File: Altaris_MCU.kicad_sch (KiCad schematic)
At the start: 94 parts, among them J1 Screw_Terminal_01x02, J10 USB_C_Receptacle_USB2.0_16P, J11 Screw_Terminal_01x02, J12 Screw_Terminal_01x02, J13 Screw_Terminal_01x02, J14 Screw_Terminal_01x02, J15 Screw_Terminal_01x02, J16 Conn_01x06, J2 Screw_Terminal_01x02, J3 Screw_Terminal_01x02, J4 Screw_Terminal_01x02, J5 Screw_Terminal_01x02, J6 Screw_Terminal_01x02, J7 Conn_01x08_Socket, J8 Screw_Terminal_01x02, J9 USB_C_Receptacle_USB2.0_16P, Q1 Q_NMOS, SW2 RESET1, SW3 BOOT1, U1 ESP32-S3-WROOM-1, U10 USBLC6-2SC6, U11 MAX31855TASA, U12 TPS62827DMQT, U13 USBLC6-2SC6, U15 CH340X, U17 MAX31855TASA, U18 MAX31855TASA, U2 MAX31855KASA, U3 TPS79333-EP, U4 ICM-20948, U5 TPS79318-EP, U6 SN74AVC4T774RSVR, U7 MAX31855KASA, U8 MAX31855KASA, U9 SN74AVC4T774RSVR

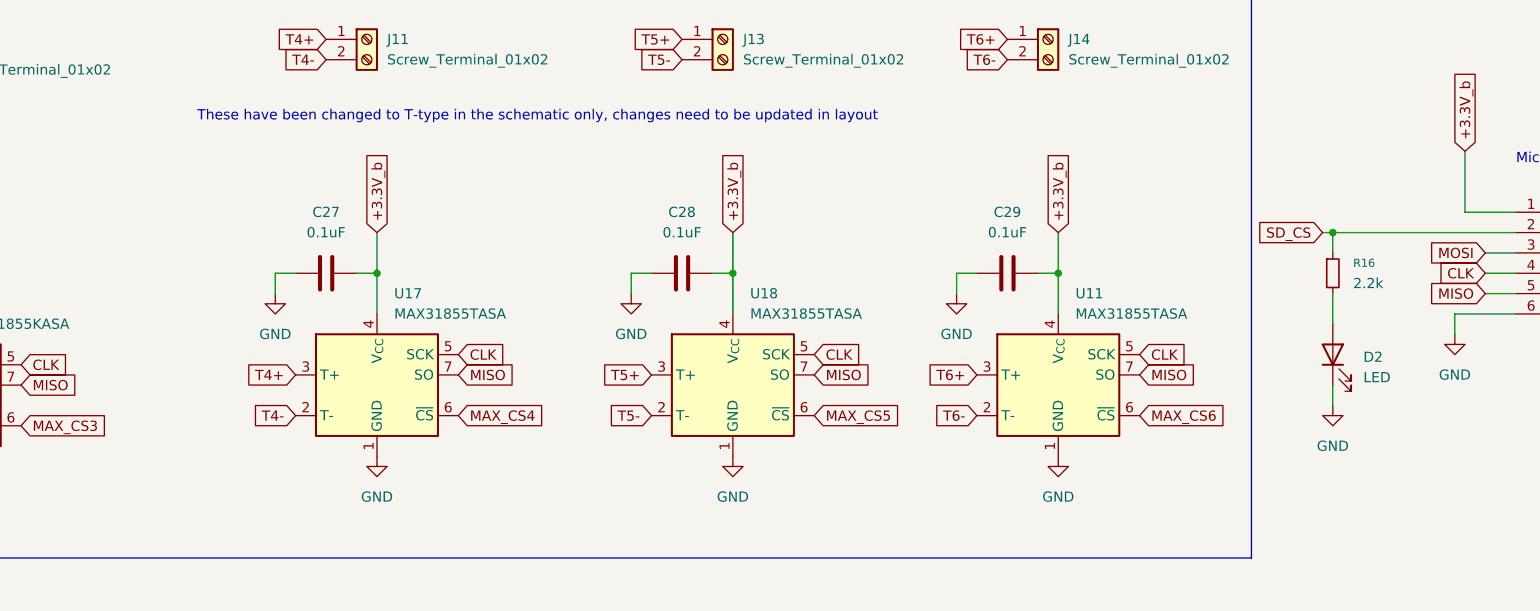
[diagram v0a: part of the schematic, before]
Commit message: added led to thermocouple power lines in schematic
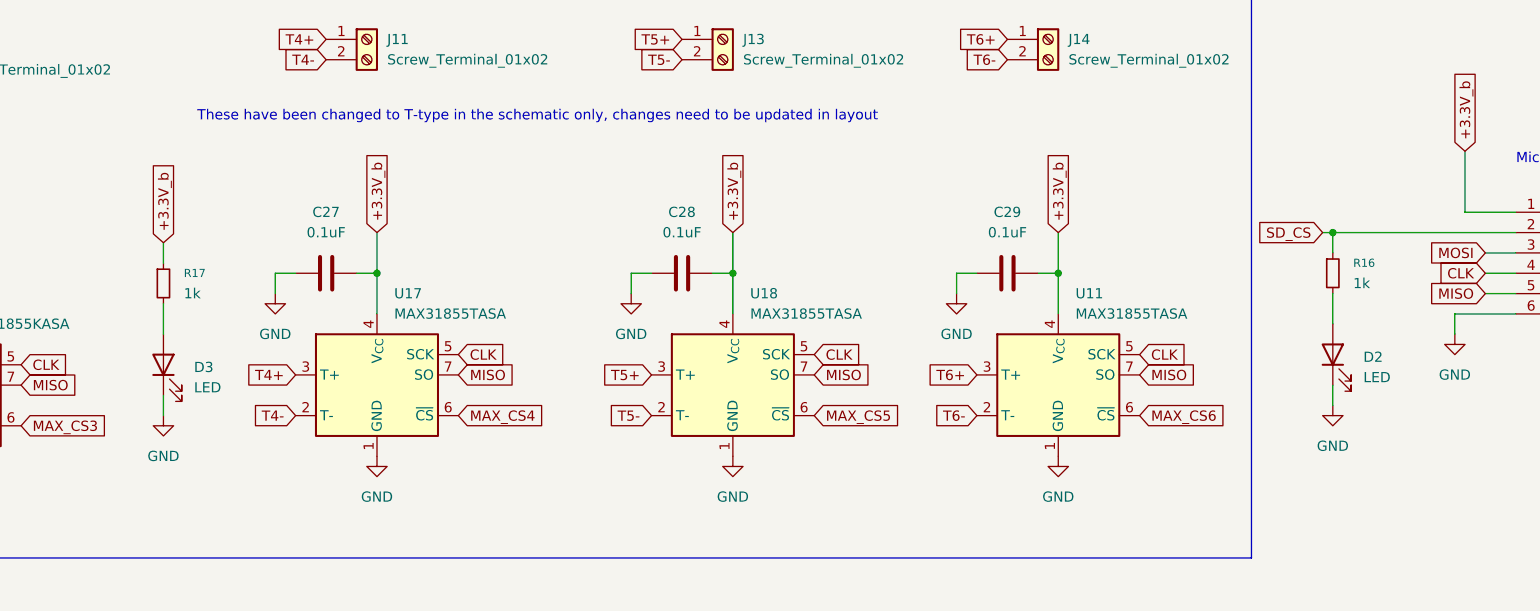
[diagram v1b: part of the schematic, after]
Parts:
- added D3: LED, LED_SMD:LED_0603_1608Metric, symbol Device:LED
- added R17: 1k, Resistor_SMD:R_0603_1608Metric, symbol Device:R_Small
- D2: footprint (none) -> LED_SMD:LED_0603_1608Metric
- R16: value 2.2k -> 1k; footprint (none) -> Resistor_SMD:R_0603_1608Metric
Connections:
- net +3.3V_b: now also R17.1
- net GND: now also D3.1 (K)
- new net: D3.2 (A), R17.2

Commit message: Cleaned up schematic, added 5V screw terminal and 3.3V buck converter, added some test led, ran DRC and fixed connections
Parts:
- removed C39, C40, C41: 0.1uF, Capacitor_SMD:C_0402_1005Metric_Pad0.74x0.62mm_HandSolder, symbol Device:C
- removed D1: 1N4148WT, Diode_SMD:D_SOD-523, symbol Diode:1N4148WT
- removed FB1: 220 @ 100MHz, Inductor_SMD:L_0402_1005Metric_Pad0.77x0.64mm_HandSolder, symbol Device:FerriteBead
- removed J10: USB_C_Receptacle_USB2.0_16P, Connector_USB:USB_C_Receptacle_HRO_TYPE-C-31-M-12, symbol Connector:USB_C_Receptacle_USB2.0_16P
- removed J12: Screw_Terminal_01x02, TerminalBlock:TerminalBlock_MaiXu_MX126-5.0-02P_1x02_P5.00mm, symbol Connector:Screw_Terminal_01x02
- removed LED1, LED2: LTST-C190KRKT, MyFootprints:LED_LTST-C190_LTO, symbol LED:LTST-C190KRKT
- removed Q1: Q_NMOS, Package_TO_SOT_SMD:SOT-23, symbol Device:Q_NMOS
- removed R13, R14: 5.1k, Resistor_SMD:R_0402_1005Metric, symbol Device:R
- removed U13: USBLC6-2SC6, Package_TO_SOT_SMD:SOT-23-6, symbol Power_Protection:USBLC6-2SC6
- removed U15: CH340X, Package_SO:MSOP-10_3x3mm_P0.5mm, symbol Interface_USB:CH340X
- removed U3: TPS79333-EP, Package_TO_SOT_SMD:SOT-23-5, symbol Regulator_Linear:TPS79333-EP
- added L2: 0.47u, MyFootprints:IND_XFL4015_COC, symbol Device:L
- added LED1, LED2, LED4: LTST-C190KRKT, LED_SMD:LED_0603_1608Metric, symbol Device:LED
- added R13, R19: 100k, Resistor_SMD:R_0402_1005Metric, symbol Device:R_Small
- added R14: 4.7k, Resistor_SMD:R_0402_1005Metric, symbol Device:R_Small
- added R18: 450k, Resistor_SMD:R_0402_1005Metric, symbol Device:R_Small
- added U3: TPS62827DMQT, MyFootprints:DMQ0006A, symbol BuckConverter:TPS62827DMQT
- C1: value 0.1uF -> 0.1u; footprint Capacitor_SMD:C_0805_2012Metric_Pad1.18x1.45mm_HandSolder -> Capacitor_SMD:C_0201_0603Metric; Distributor Link 1 (none) -> https://www.mouser.com/ProductDetail/Samsung-Electro-Mechan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; Distributor Link 2 (none) -> https://www.digikey.com/en/products/detail/samsung-electro-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; LCSC C28233 -> C1525; Manufacturer (none) -> Samsung; Manufacturer Part Number (none) -> CL05B104KO5NNNC
- C10: value 10uF -> 120p; footprint Capacitor_SMD:C_0805_2012Metric_Pad1.18x1.45mm_HandSolder -> Capacitor_SMD:C_0201_0603Metric; Distributor Link 1 (none) -> https://www.mouser.com/ProductDetail/Samsung-Electro-Mechan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; Distributor Link 2 (none) -> https://www.digikey.com/en/products/detail/samsung-electro-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; LCSC C28233 -> C1525; Manufacturer (none) -> Samsung; Manufacturer Part Number (none) -> CL05B104KO5NNNC
- C5: value 0.01uF -> 4.7u; footprint Capacitor_SMD:C_0805_2012Metric_Pad1.18x1.45mm_HandSolder -> Capacitor_SMD:C_0201_0603Metric; Distributor Link 1 (none) -> https://www.mouser.com/ProductDetail/Samsung-Electro-Mechan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; Distributor Link 2 (none) -> https://www.digikey.com/en/products/detail/samsung-electro-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; LCSC C28233 -> C1525; Manufacturer (none) -> Samsung; Manufacturer Part Number (none) -> CL05B104KO5NNNC
- C7: value 10uF -> 30u; footprint Capacitor_SMD:C_0805_2012Metric_Pad1.18x1.45mm_HandSolder -> Capacitor_SMD:C_0201_0603Metric; Distributor Link 1 (none) -> https://www.mouser.com/ProductDetail/Samsung-Electro-Mechan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; Distributor Link 2 (none) -> https://www.digikey.com/en/products/detail/samsung-electro-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; LCSC C15850 -> C1525; Manufacturer (none) -> Samsung; Manufacturer Part Number (none) -> CL05B104KO5NNNC
- LED3: renamed from D3; value LED -> LTST-C190KRKT
- R11: value 1k -> 4.7k
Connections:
- net +3.3V_b: now also C10.1, C7.1, L2.2, R18.2; no longer C7.2
- net +5V_b: now also C1.2, C5.2, R13.2, U3.1 (EN), U3.6 (VIN)
- net ADC_IN1: now also U1.22 (IO14); no longer U1.23 (IO21)
- net ADC_IN2: now also U1.23 (IO21); no longer U1.24 (IO47)
- net ADC_IN3: now also U1.24 (IO47); no longer U1.25 (IO48)
- net ADC_IN4: now also U1.25 (IO48); no longer U1.26 (IO45)
- net GND: now also C7.2, LED1.1 (K), LED2.1 (K), LED4.1 (K), R19.1, U3.4 (GND); no longer C10.1, C7.1
- net TESTLED: now also U1.11 (IO18); no longer U1.22 (IO14)
- net at R12.1: now also LED4.2 (A)
- net at C10.2: now also R18.1, R19.2, U3.3 (FB); no longer C1.2
- net at R11.1: now also LED2.2 (A)
- new net: LED1.2 (A), R14.1
- new net: R13.1, R14.2, U3.2 (PG)
- new net: L2.1, U3.5 (SW)
- no-connect marks 26 -> 21
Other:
- note removed: "2SK3018"
- note removed: "USB to Serial Port Chip"
- note removed: "WILL PROBOLY GET RID OF THIS LDO"
- note removed: "WILL PROBS GET RID OF THIS PORT"
- moved on the sheet: C4, C6, C8, C9, FB2, J8, U5

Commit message: finalized pcb
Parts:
- removed J7: Conn_01x08_Socket, Connector_PinHeader_2.54mm:PinHeader_2x04_P2.54mm_Vertical, symbol Connector:Conn_01x08_Socket
- added LED5: LTST-C190KRKT, LED_SMD:LED_0603_1608Metric, symbol Device:LED
- added R20: 1k, Resistor_SMD:R_0402_1005Metric, symbol Device:R_Small
- D2: value LED -> LTST-C190KRKT
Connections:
- net GND: now also LED5.1 (K)
- net SD_CS: now also U1.12 (IO8); no longer U1.5 (IO5)
- net at C4.2, C9.2, FB2.1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: now also R20.2
- net RXD0: no longer names the net of U1.36 (RXD0)
- net TXD0: no longer names the net of U1.37 (TXD0)
- new net: LED5.2 (A), R20.1
- no-connect marks 21 -> 23
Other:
- note removed: "Debug"
- moved on the sheet: FB2

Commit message: final pcb
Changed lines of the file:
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@@
 	)
 	(junction
+		(at 397.51 234.95)
+		(diameter 0)
+		(color 0 0 0 0)
+	)
+	(junction
 		(at 445.77 46.99)
 		(diameter 0)
@@
 					(unit 1)
 				)
+			)
+		)
+	)
+	(symbol
+		(lib_id "power:PWR_FLAG")
+		(at 397.51 234.95 0)
+		(unit 1)
+		(exclude_from_sim no)
+		(in_bom yes)
+		(on_board yes)
+		(dnp no)
+		(fields_autoplaced yes)
+		(property "Reference" "#FLG07"
+			(at 397.51 233.045 0)
+			(effects
+				(font
+					(size 1.27 1.27)
+				)
+				(hide yes)
+			)
+		)
+		(property "Value" "PWR_FLAG"
+			(at 397.51 229.87 0)
+			(effects
+				(font
+					(size 1.27 1.27)
+				)
+				(hide yes)
+			)
+		)
+		(property "Footprint" ""
+			(at 397.51 234.95 0)
+			(effects
+				(font
+					(size 1.27 1.27)
+				)
+				(hide yes)
+			)
+		)
+		(property "Datasheet" "~"
+			(at 397.51 234.95 0)
+			(effects
+				(font
+					(size 1.27 1.27)
+				)
+				(hide yes)
+			)
+		)
+		(property "Description" "Special symbol for telling ERC where power comes from"
+			(at 397.51 234.95 0)
+			(effects
+				(font
+					(size 1.27 1.27)
+				)
+				(hide yes)
+			)
+		)
+		(pin "1"
+		)
+		(instances
+			(project "Altaris_MCU"
+				(path "/21889916-6808-460c-a148-21d1f170ea7e"
+					(reference "#FLG07")
+					(unit 1)
+				)

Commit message: pcb final 1
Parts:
- added LED6: LTST-C190KRKT, LED_SMD:LED_0603_1608Metric, symbol Device:LED
- added R21: 1k, Resistor_SMD:R_0603_1608Metric, symbol Device:R_Small
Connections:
- net +3.3V_b: now also R21.1
- net GND: now also LED6.1 (K)
- new net: LED6.2 (A), R21.2

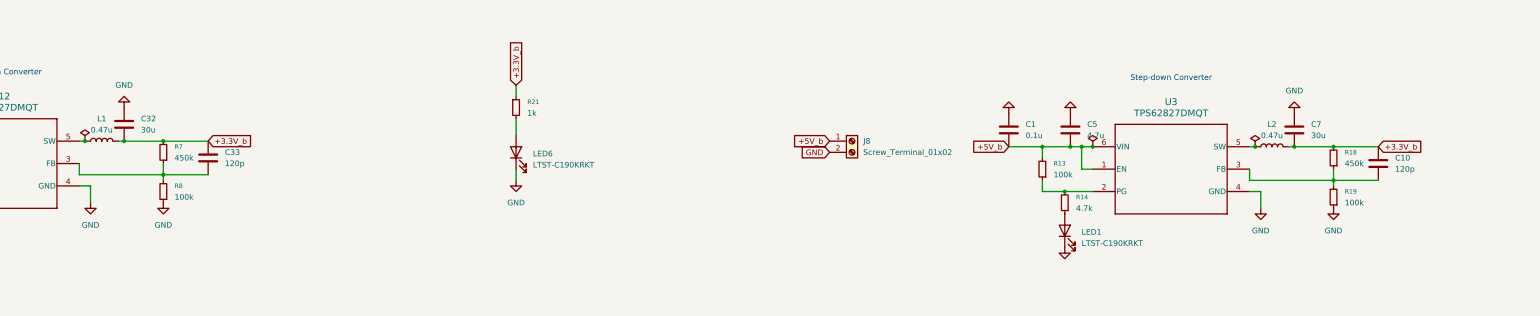
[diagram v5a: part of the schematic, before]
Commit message: edited capcitors
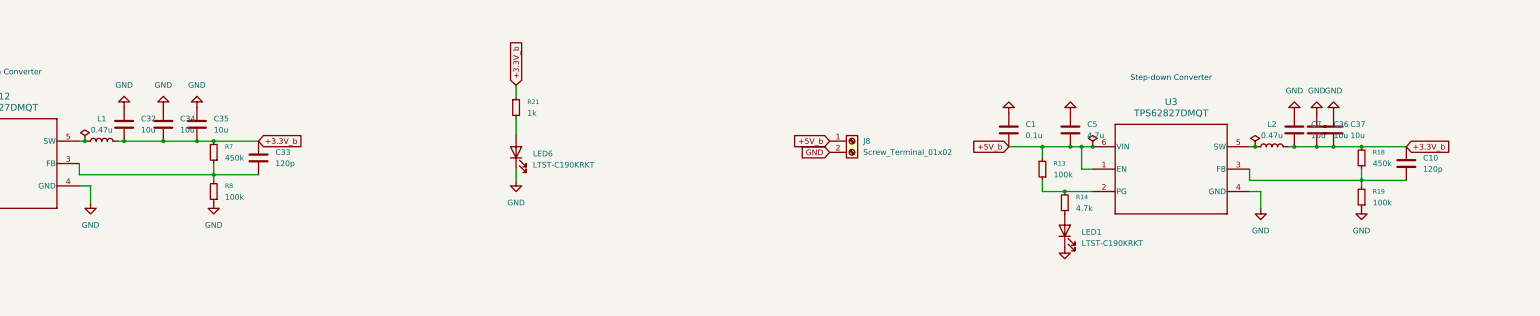
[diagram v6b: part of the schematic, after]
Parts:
- added C34, C35, C36, C37: 10u, Capacitor_SMD:C_0201_0603Metric, symbol Device:C
- C32, C7: value 30u -> 10u
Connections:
- net +3.3V_b: now also C34.1, C35.1, C36.1, C37.1
- net GND: now also C34.2, C35.2, C36.2, C37.2
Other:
- moved on the sheet: C10, C33, R18, R19, R7, R8
